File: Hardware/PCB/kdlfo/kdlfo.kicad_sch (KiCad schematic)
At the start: 21 parts, among them J1 3_pin_Molex_header, J15 Synth_power_2x5, J2 3_pin_Molex_header, J3 3_pin_Molex_header, J5 3_pin_Molex_connector, J6 3_pin_Molex_connector, J7 3_pin_Molex_header

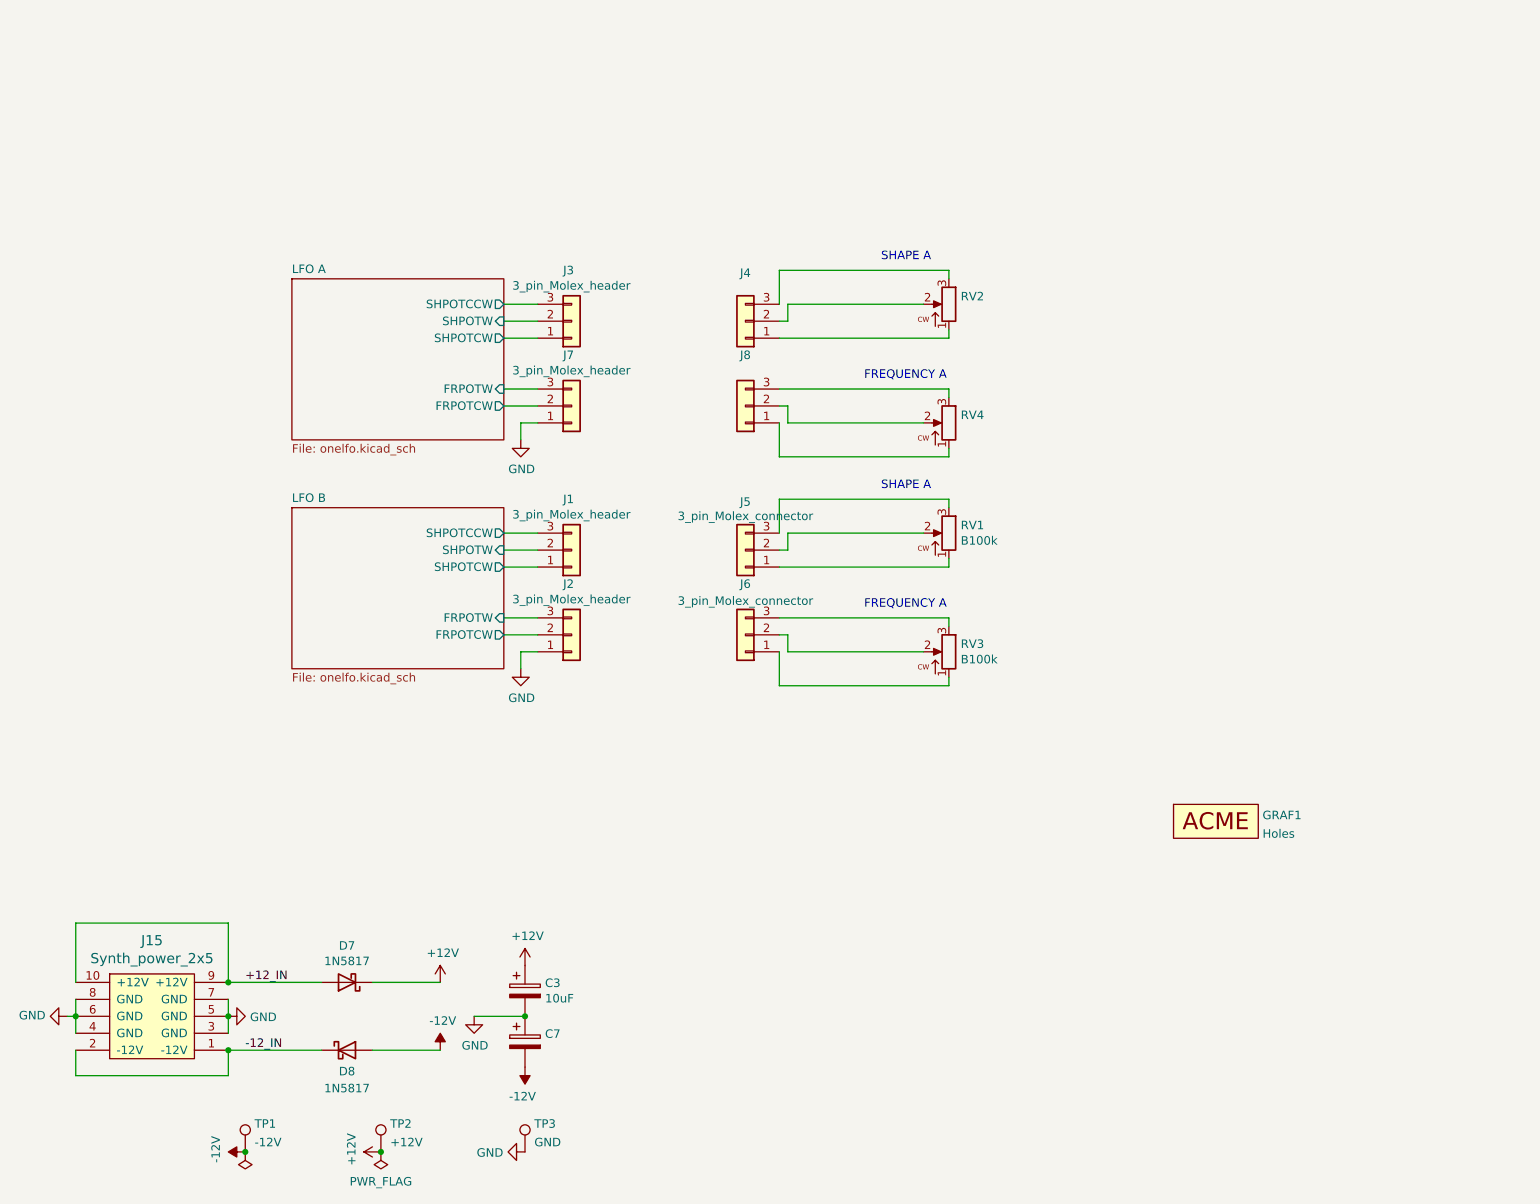
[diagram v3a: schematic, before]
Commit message: Reorg schematic, redo layout some more
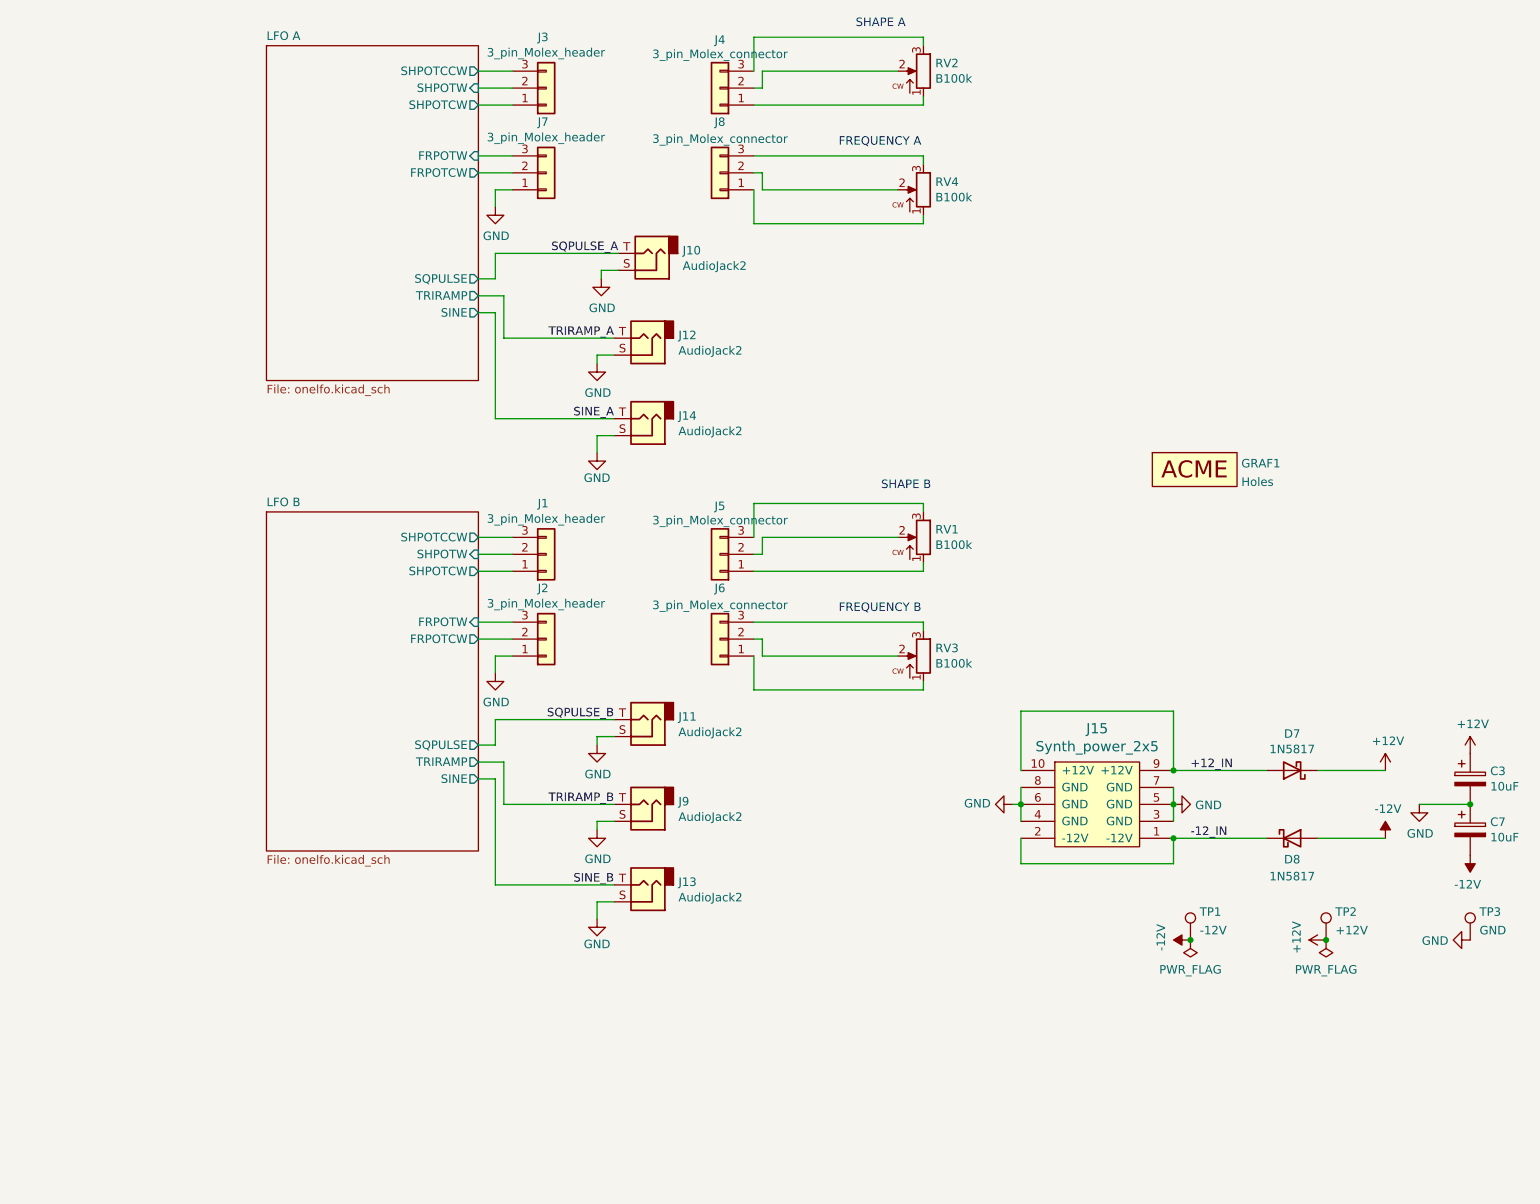
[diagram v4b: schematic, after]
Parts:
- added J10, J11, J12, J13, J14, J9: AudioJack2, ao_tht:Jack_6.35mm_PJ_629HAN, symbol Connector:AudioJack2
- C7: value (none) -> 10uF
- J4, J8: value (none) -> 3_pin_Molex_connector
- RV2, RV4: value (none) -> B100k; footprint (none) -> ao_tht:Potentiometer_Alpha_16mm_Single_Vertical
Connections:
- net GND: now also J10.S, J11.S, J12.S, J13.S, J14.S, J9.S
- new net SINE_A: J14.T
- new net SINE_B: J13.T
- new net SQPULSE_A: J10.T
- new net SQPULSE_B: J11.T
- new net TRIRAMP_A: J12.T
- new net TRIRAMP_B: J9.T
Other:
- sheet LFO A ports: added SINE, SQPULSE, TRIRAMP; removed none
- sheet LFO B ports: added SINE, SQPULSE, TRIRAMP; removed none
- note added: "FREQUENCY B"
- note added: "SHAPE B"
- moved on the sheet: C3, C7, D7, D8, GRAF1, J1, J15, J2, J3, J4, J5, J6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

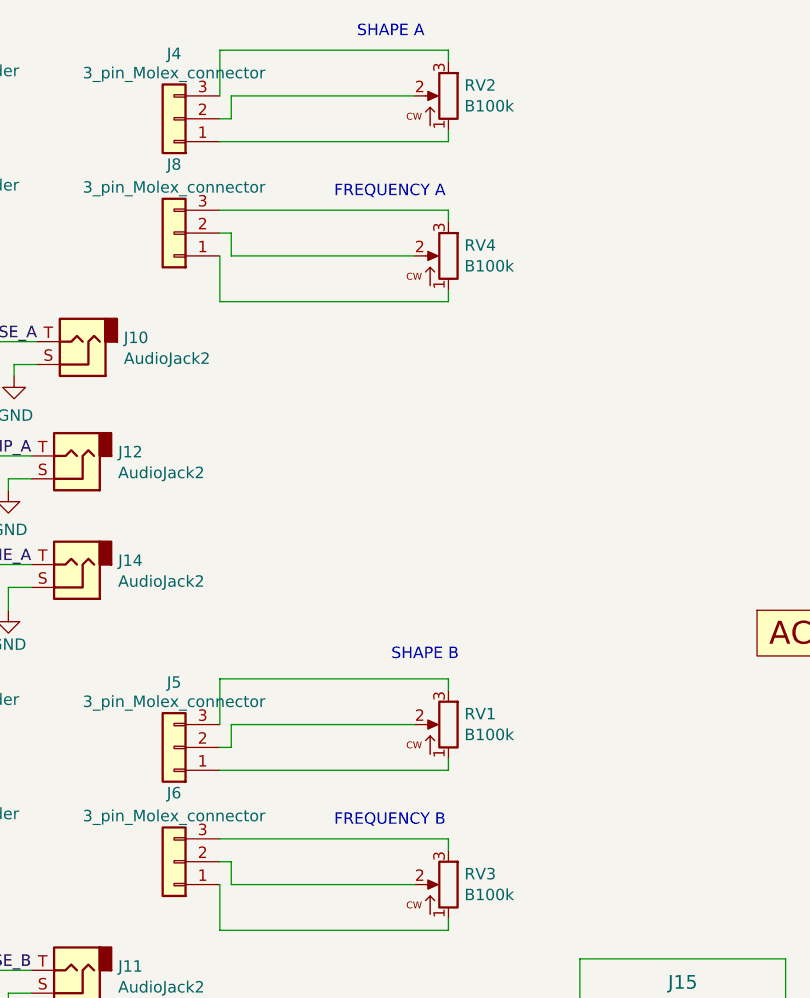
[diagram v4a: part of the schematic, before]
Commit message: Fix LED
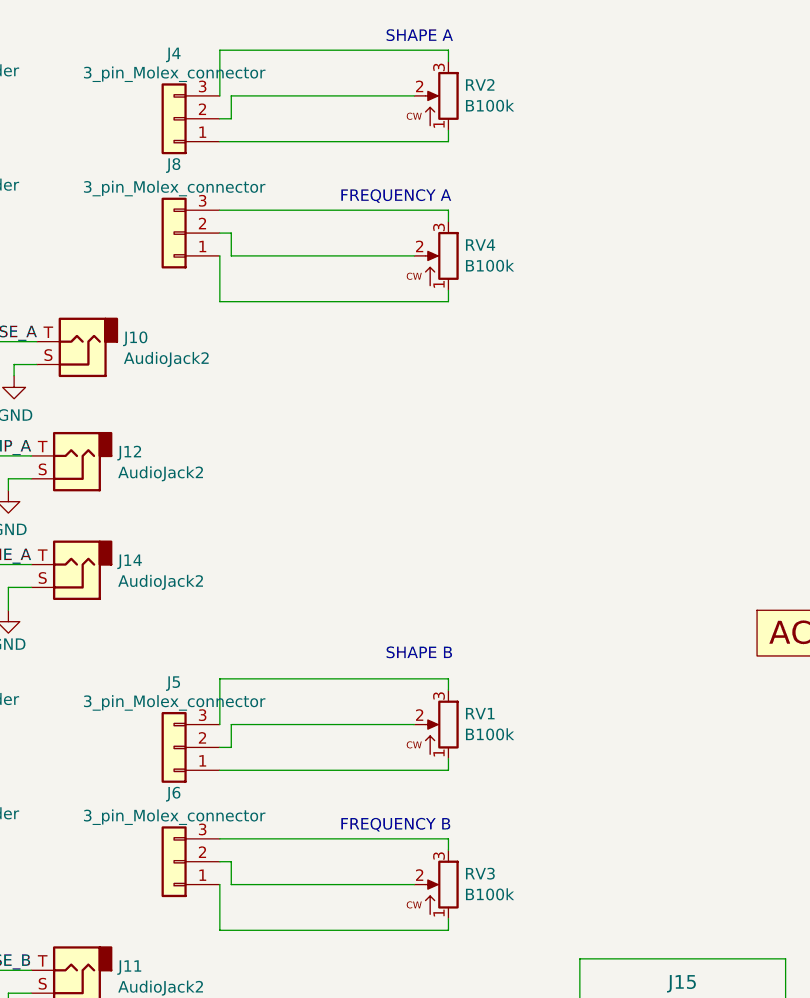
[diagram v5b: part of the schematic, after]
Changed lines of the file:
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@@
     (stroke (width 0) (type default) (color 0 0 0 0))
   )
-  (text "SHAPE A" (at 151.765 23.495 0)
+  (text "SHAPE A" (at 154.94 24.13 0)
     (effects (font (size 1.27 1.27)) (justify left bottom))
   )
-  (text "FREQUENCY B" (at 149.225 111.125 0)
+  (text "FREQUENCY B" (at 149.86 111.76 0)
     (effects (font (size 1.27 1.27)) (justify left bottom))
   )
-  (text "SHAPE B" (at 155.575 92.71 0)
+  (text "SHAPE B" (at 154.94 92.71 0)
     (effects (font (size 1.27 1.27)) (justify left bottom))
   )
-  (text "FREQUENCY A" (at 149.225 41.275 0)
+  (text "FREQUENCY A" (at 149.86 41.91 0)
     (effects (font (size 1.27 1.27)) (justify left bottom))
   )
@@
       (reference "#PWR015") (unit 1) (value "GND") (footprint "")
     )
-    (path "/dd04668a-5239-4bd2-ae67-038a463e12dc/2338658c-a171-455d-ad40-3e03c5e2e649"
+    (path "/dd04668a-5239-4bd2-ae67-038a463e12dc/fdf94941-cfd6-457e-ab4d-afeea3ed65a6"
       (reference "#PWR016") (unit 1) (value "GND") (footprint "")
     )
@@
       (reference "#PWR017") (unit 1) (value "GND") (footprint "")
     )
-    (path "/8c42dada-182a-49c1-bf92-143204f6b7ba/2338658c-a171-455d-ad40-3e03c5e2e649"
+    (path "/8c42dada-182a-49c1-bf92-143204f6b7ba/fdf94941-cfd6-457e-ab4d-afeea3ed65a6"
       (reference "#PWR018") (unit 1) (value "GND") (footprint "")
     )
@@
     )
     (path "/8c42dada-182a-49c1-bf92-143204f6b7ba/12a1f0d0-f85d-44de-8a13-dbeb72a868b4"
-      (reference "C1") (unit 1) (value "220n") (footprint "ao_tht:C_Rect_L7.2mm_W7.2mm_P5.00mm_FKS2_FKP2_MKS2_MKP2")
+      (reference "C1") (unit 1) (value "220n/2.2uF") (footprint "ao_tht:C_Rect_L7.2mm_W7.2mm_P5.00mm_FKS2_FKP2_MKS2_MKP2")
     )
     (path "/dd04668a-5239-4bd2-ae67-038a463e12dc/12a1f0d0-f85d-44de-8a13-dbeb72a868b4"
-      (reference "C2") (unit 1) (value "220n") (footprint "ao_tht:C_Rect_L7.2mm_W7.2mm_P5.00mm_FKS2_FKP2_MKS2_MKP2")
+      (reference "C2") (unit 1) (value "220n/2.2uF") (footprint "ao_tht:C_Rect_L7.2mm_W7.2mm_P5.00mm_FKS2_FKP2_MKS2_MKP2")
     )
     (path "/00000000-0000-0000-0000-00005f73fa30"
@@
       (reference "R13") (unit 1) (value "10k") (footprint "ao_tht:R_Axial_DIN0207_L6.3mm_D2.5mm_P10.16mm_Horizontal")
     )
-    (path "/dd04668a-5239-4bd2-ae67-038a463e12dc/c72de2df-7932-4fee-8e71-8d34991e36d4"
-      (reference "R14") (unit 1) (value "4.7k") (footprint "ao_tht:R_Axial_DIN0207_L6.3mm_D2.5mm_P10.16mm_Horizontal")
+    (path "/dd04668a-5239-4bd2-ae67-038a463e12dc/544942af-4bc8-48f9-ade9-436e47b2d059"
+      (reference "R14") (unit 1) (value "RL") (footprint "ao_tht:R_Axial_DIN0207_L6.3mm_D2.5mm_P10.16mm_Horizontal")
     )
     (path "/8c42dada-182a-49c1-bf92-143204f6b7ba/9b02c8c3-9246-4b4e-8eeb-02118d4739fa"
@@
       (reference "R27") (unit 1) (value "2.2k") (footprint "ao_tht:R_Axial_DIN0207_L6.3mm_D2.5mm_P10.16mm_Horizontal")
     )
-    (path "/8c42dada-182a-49c1-bf92-143204f6b7ba/c72de2df-7932-4fee-8e71-8d34991e36d4"
-      (reference "R28") (unit 1) (value "4.7k") (footprint "ao_tht:R_Axial_DIN0207_L6.3mm_D2.5mm_P10.16mm_Horizontal")
+    (path "/8c42dada-182a-49c1-bf92-143204f6b7ba/544942af-4bc8-48f9-ade9-436e47b2d059"
+      (reference "R28") (unit 1) (value "RL") (footprint "ao_tht:R_Axial_DIN0207_L6.3mm_D2.5mm_P10.16mm_Horizontal")
     )
     (path "/dd04668a-5239-4bd2-ae67-038a463e12dc/101b9162-4dd2-4598-8eb9-9b7e9c3ad37f"

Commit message: Final pre fab tweaks, Gerbers
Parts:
- added C1: (no value), ao_tht:C_Rect_L7.2mm_W7.2mm_P5.00mm_FKS2_FKP2_MKS2_MKP2, symbol Device:C
- added C2: (no value), symbol ao_symbols:C
- added GRAF2, GRAF3: (no value), symbol ao_symbols:Graphic
- renumbered C7 to C4, D7 to D1, D8 to D2, J3 to J1, J4 to J11, J8 to J12, J5 to J13, J6 to J14, J7 to J2, J1 to J3, J2 to J4, J12 to J5, J14 to J6, J11 to J7, J9 to J8, J13 to J9, RV2 to RV1, RV4 to RV2, RV1 to RV3, RV3 to RV4
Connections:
- net LFO A/FRPOTCW: now also J2.3 (Pin_3); no longer J2.2 (Pin_2)
- net LFO A/FRPOTW: now also J2.2 (Pin_2); no longer J2.3 (Pin_3)
- net LFO A/SHPOTCCW: now also J1.1 (Pin_1); no longer J1.3 (Pin_3)
- net LFO A/SHPOTCW: now also J1.3 (Pin_3); no longer J1.1 (Pin_1)
- net LFO B/FRPOTCW: now also J4.3 (Pin_3); no longer J4.2 (Pin_2)
- net LFO B/FRPOTW: now also J4.2 (Pin_2); no longer J4.3 (Pin_3)
- net LFO B/SHPOTCCW: now also J3.1 (Pin_1); no longer J3.3 (Pin_3)
- net LFO B/SHPOTCW: now also J3.3 (Pin_3); no longer J3.1 (Pin_1)
- new net LFO A/CAP1: C1.1
- new net LFO A/CAP2: C1.2
- new net LFO B/CAP1: C2.1
- new net LFO B/CAP2: C2.2
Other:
- sheet LFO A ports: added CAP1, CAP2; removed none
- sheet LFO B ports: added CAP1, CAP2; removed none
- moved on the sheet: GRAF1

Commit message: Slotted jack footprints you idiot
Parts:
- C1: value (none) -> 220n
- C2: value (none) -> 2.2uF; footprint (none) -> ao_tht:C_Radial_D5.0mm_H11.0mm_P2.00mm
- GRAF2: value (none) -> CC0 logo; footprint (none) -> ao_tht:CC0_logo
- GRAF3: value (none) -> AO logo; footprint (none) -> ao_tht:analogoutput_12mm
- J10, J5, J6, J7, J8, J9: footprint ao_tht:Jack_6.35mm_PJ_629HAN -> (none)
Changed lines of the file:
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@@
       (effects (font (size 1.27 1.27)) (justify right))
     )
-    (property "Footprint" "ao_tht:Jack_6.35mm_PJ_629HAN" (id 2) (at 121.285 57.15 0)
+    (property "Footprint" "" (id 2) (at 121.285 57.15 0)
       (effects (font (size 1.27 1.27)) hide)
     )
@@
       (effects (font (size 1.27 1.27)) (justify right))
     )
-    (property "Footprint" "ao_tht:Jack_6.35mm_PJ_629HAN" (id 2) (at 120.65 151.765 0)
+    (property "Footprint" "" (id 2) (at 120.65 151.765 0)
       (effects (font (size 1.27 1.27)) hide)
     )
@@
       (effects (font (size 1.27 1.27)) (justify left))
     )
-    (property "Value" "" (id 1) (at 52.451 124.8922 0)
-      (effects (font (size 1.27 1.27)) (justify left))
-    )
-    (property "Footprint" "" (id 2) (at 50.4952 127 0)
+    (property "Value" "2.2uF" (id 1) (at 52.451 124.8922 0)
+      (effects (font (size 1.27 1.27)) (justify left))
+    )
+    (property "Footprint" "ao_tht:C_Radial_D5.0mm_H11.0mm_P2.00mm" (id 2) (at 50.4952 127 0)
       (effects (font (size 1.27 1.27)) hide)
     )
@@
     (in_bom yes) (on_board yes)
     (property "Reference" "C1" (id 0) (at 54.61 52.07 0))
-    (property "Value" "" (id 1) (at 54.61 54.3814 0))
+    (property "Value" "220n" (id 1) (at 54.61 54.3814 0))
     (property "Footprint" "ao_tht:C_Rect_L7.2mm_W7.2mm_P5.00mm_FKS2_FKP2_MKS2_MKP2" (id 2) (at 50.4952 57.15 0)
       (effects (font (size 1.27 1.27)) hide)
@@
       (effects (font (size 1.27 1.27)) (justify right))
     )
-    (property "Footprint" "ao_tht:Jack_6.35mm_PJ_629HAN" (id 2) (at 120.65 69.85 0)
+    (property "Footprint" "" (id 2) (at 120.65 69.85 0)
       (effects (font (size 1.27 1.27)) hide)
     )
@@
       (effects (font (size 1.27 1.27)) (justify right))
     )
-    (property "Footprint" "ao_tht:Jack_6.35mm_PJ_629HAN" (id 2) (at 120.65 127 0)
+    (property "Footprint" "" (id 2) (at 120.65 127 0)
       (effects (font (size 1.27 1.27)) hide)
     )
@@
       (effects (font (size 1.27 1.27)) (justify right))
     )
-    (property "Footprint" "ao_tht:Jack_6.35mm_PJ_629HAN" (id 2) (at 120.65 81.915 0)
+    (property "Footprint" "" (id 2) (at 120.65 81.915 0)
       (effects (font (size 1.27 1.27)) hide)
     )
@@
       (effects (font (size 1.27 1.27)) (justify left))
     )
-    (property "Value" "" (id 1) (at 210.185 98.3866 0)
-      (effects (font (size 1.27 1.27)) (justify left))
-    )
-    (property "Footprint" "" (id 2) (at 203.2 96.52 0)
+    (property "Value" "CC0 logo" (id 1) (at 210.185 98.3866 0)
+      (effects (font (size 1.27 1.27)) (justify left))
+    )
+    (property "Footprint" "ao_tht:CC0_logo" (id 2) (at 203.2 96.52 0)
       (effects (font (size 1.27 1.27)) hide)
     )
@@
       (effects (font (size 1.27 1.27)) (justify right))
     )
-    (property "Footprint" "ao_tht:Jack_6.35mm_PJ_629HAN" (id 2) (at 120.65 139.7 0)
+    (property "Footprint" "" (id 2) (at 120.65 139.7 0)
       (effects (font (size 1.27 1.27)) hide)
     )
@@
       (effects (font (size 1.27 1.27)) (justify left))
     )
-    (property "Value" "" (id 1) (at 210.185 104.7366 0)
-      (effects (font (size 1.27 1.27)) (justify left))
-    )
-    (property "Footprint" "" (id 2) (at 203.2 102.87 0)
+    (property "Value" "AO logo" (id 1) (at 210.185 104.7366 0)
+      (effects (font (size 1.27 1.27)) (justify left))
+    )
+    (property "Footprint" "ao_tht:analogoutput_12mm" (id 2) (at 203.2 102.87 0)
       (effects (font (size 1.27 1.27)) hide)
     )
@@
     )
     (path "/a424e5ab-9cfc-4bb8-a430-30011c17f1e2"
-      (reference "J5") (unit 1) (value "AudioJack2") (footprint "ao_tht:Jack_6.35mm_PJ_629HAN")
+      (reference "J5") (unit 1) (value "AudioJack2") (footprint "ao_tht:Jack_6.35mm_PJ_629HAN_slots")
     )
     (path "/db2c1246-0e80-4909-8fbb-6e60c0910160"
-      (reference "J6") (unit 1) (value "AudioJack2") (footprint "ao_tht:Jack_6.35mm_PJ_629HAN")
+      (reference "J6") (unit 1) (value "AudioJack2") (footprint "ao_tht:Jack_6.35mm_PJ_629HAN_slots")
     )
     (path "/d75f1129-bee5-4ab7-81cd-7c7bcd3583a9"
-      (reference "J7") (unit 1) (value "AudioJack2") (footprint "ao_tht:Jack_6.35mm_PJ_629HAN")
+      (reference "J7") (unit 1) (value "AudioJack2") (footprint "ao_tht:Jack_6.35mm_PJ_629HAN_slots")
     )
     (path "/f414999d-04e2-4740-b33b-f7fedf64b617"
-      (reference "J8") (unit 1) (value "AudioJack2") (footprint "ao_tht:Jack_6.35mm_PJ_629HAN")
+      (reference "J8") (unit 1) (value "AudioJack2") (footprint "ao_tht:Jack_6.35mm_PJ_629HAN_slots")
     )
     (path "/20bb75ea-9649-462e-87bc-e4875dd5dc93"
-      (reference "J9") (unit 1) (value "AudioJack2") (footprint "ao_tht:Jack_6.35mm_PJ_629HAN")
+      (reference "J9") (unit 1) (value "AudioJack2") (footprint "ao_tht:Jack_6.35mm_PJ_629HAN_slots")
     )
     (path "/0eded119-8009-4729-a4f0-52acb4202868"
-      (reference "J10") (unit 1) (value "AudioJack2") (footprint "ao_tht:Jack_6.35mm_PJ_629HAN")
+      (reference "J10") (unit 1) (value "AudioJack2") (footprint "ao_tht:Jack_6.35mm_PJ_629HAN_slots")
     )
     (path "/f01e3e4e-8e61-4043-9d48-b0a11f6fd3a9"
